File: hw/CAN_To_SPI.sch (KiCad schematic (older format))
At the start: 15 parts

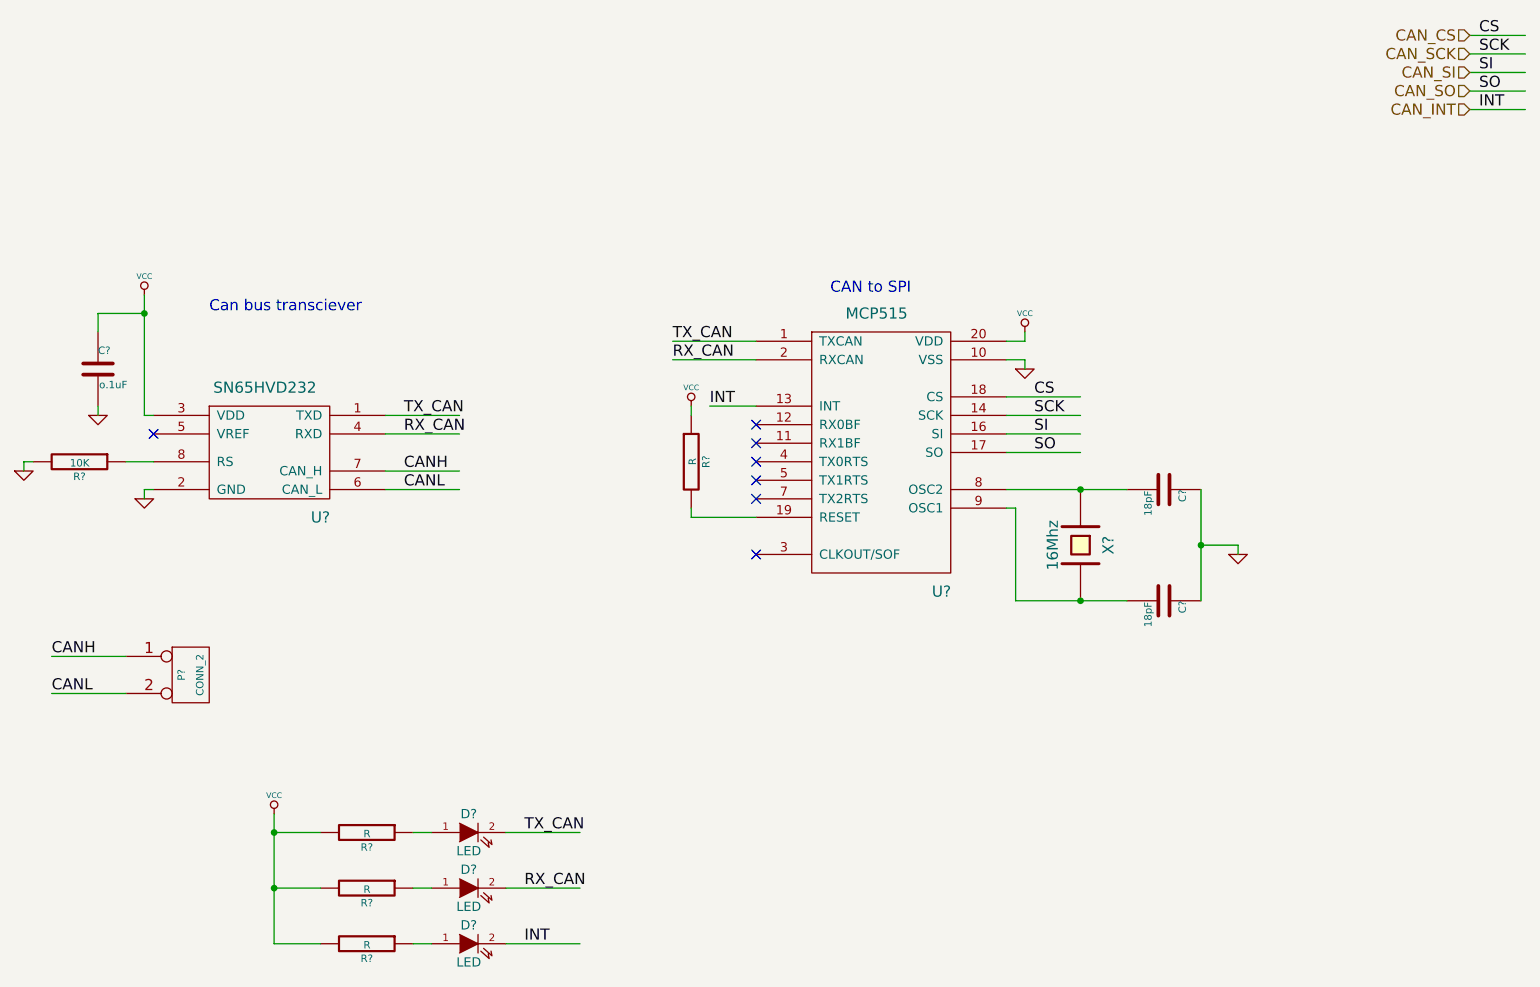
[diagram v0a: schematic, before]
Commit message: Added some of the netlist
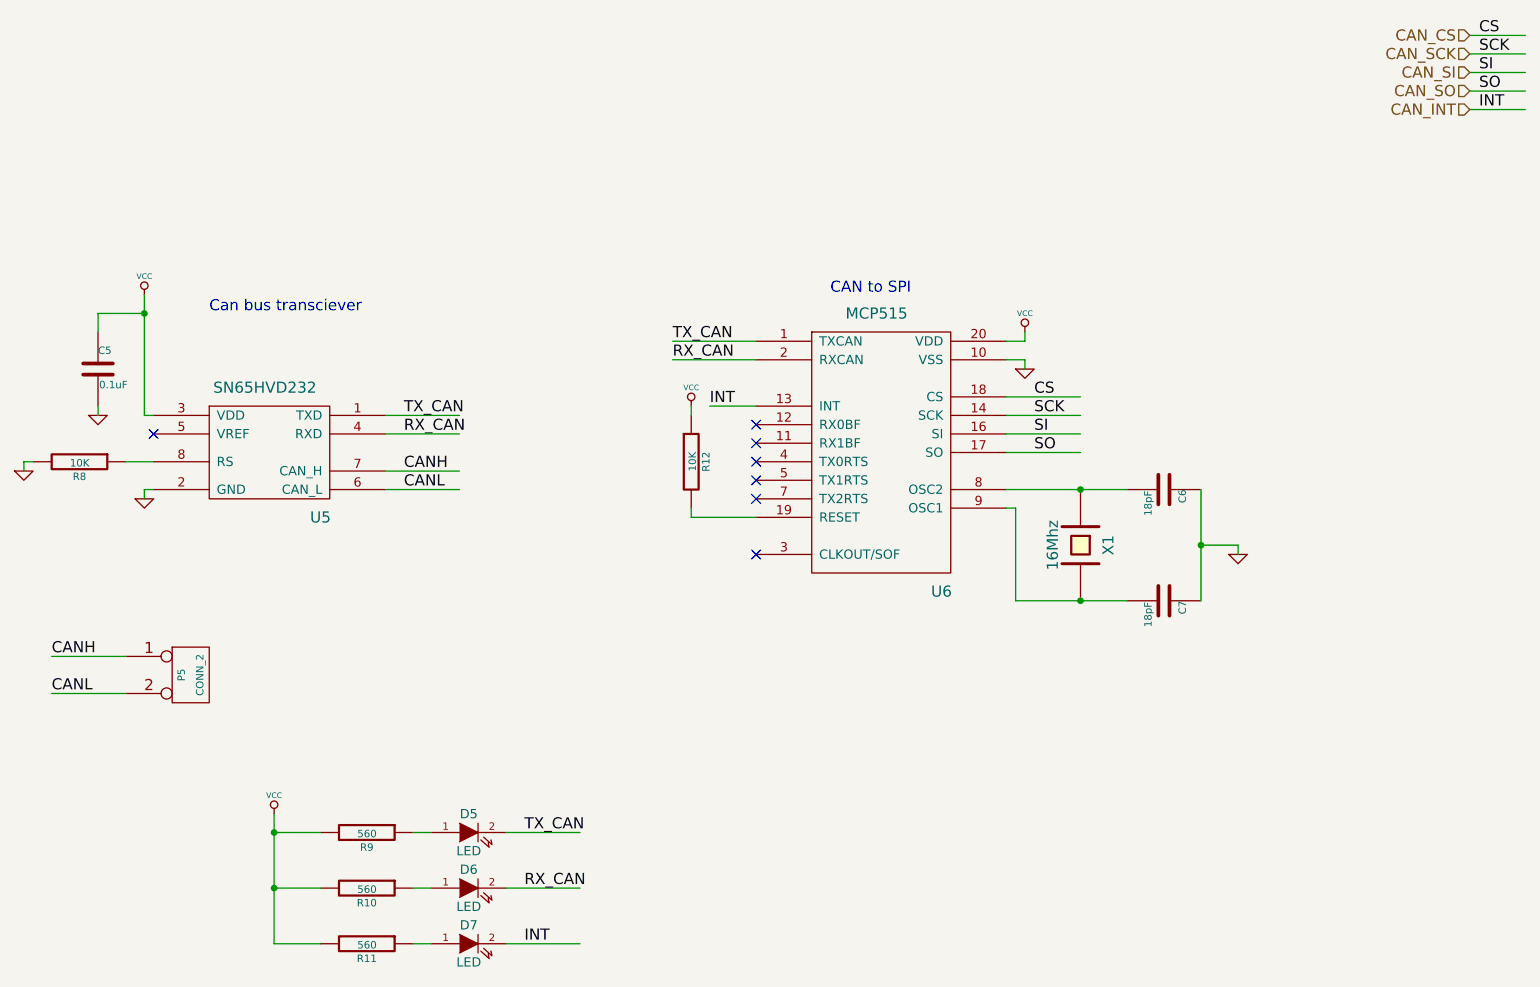
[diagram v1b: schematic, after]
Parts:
- C5: renamed from C?; value o.1uF -> 0.1uF
- R10, R11, R9: renamed from R?; value R -> 560
- R12: renamed from R?; value R -> 10K
- gave numbers to parts that had none: 10
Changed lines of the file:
@@
 LIBS:10to7_sensors
 LIBS:10to7_ic
+LIBS:Stepstick-cache
 EELAYER 24 0
 EELAYER END
@@
 $EndDescr
 $Comp
-L MCP2551 U?
+L MCP2551 U5
 U 1 1 538B0DEC
 P 3800 3600
-F 0 "U?" H 4100 3200 60  0000 C CNN
+F 0 "U5" H 4100 3200 60  0000 C CNN
 F 1 "SN65HVD232" H 3800 3900 60  0000 C CNN
 F 2 "" H 3800 3600 60  0000 C CNN
@@
 	3150 3850 3150 3900
 $Comp
-L GND #PWR?
+L GND #PWR031
 U 1 1 538B0DF4
 P 3150 3900
-F 0 "#PWR?" H 3150 3900 30  0001 C CNN
+F 0 "#PWR031" H 3150 3900 30  0001 C CNN
 F 1 "GND" H 3150 3830 30  0001 C CNN
 F 2 "" H 3150 3900 60  0000 C CNN
@@
 	3200 3700 3050 3700
 $Comp
-L R R?
+L R R8
 U 1 1 538B0DFD
 P 2800 3700
-F 0 "R?" V 2880 3700 40  0000 C CNN
+F 0 "R8" V 2880 3700 40  0000 C CNN
 F 1 "10K" V 2807 3701 40  0000 C CNN
 F 2 "" V 2730 3700 30  0000 C CNN
@@
 	2500 3700 2500 3750
 $Comp
-L GND #PWR?
+L GND #PWR032
 U 1 1 538B0E05
 P 2500 3750
-F 0 "#PWR?" H 2500 3750 30  0001 C CNN
+F 0 "#PWR032" H 2500 3750 30  0001 C CNN
 F 1 "GND" H 2500 3680 30  0001 C CNN
 F 2 "" H 2500 3750 60  0000 C CNN
@@
 RX_CAN
 $Comp
-L C C?
+L C C5
 U 1 1 538B0E14
 P 2900 3200
-F 0 "C?" H 2900 3300 40  0000 L CNN
-F 1 "o.1uF" H 2906 3115 40  0000 L CNN
+F 0 "C5" H 2900 3300 40  0000 L CNN
+F 1 "0.1uF" H 2906 3115 40  0000 L CNN
 F 2 "" H 2938 3050 30  0000 C CNN
 F 3 "" H 2900 3200 60  0000 C CNN
@@
 	2900 3400 2900 3450
 $Comp
-L GND #PWR?
+L GND #PWR033
 U 1 1 538B0E1E
 P 2900 3450
-F 0 "#PWR?" H 2900 3450 30  0001 C CNN
+F 0 "#PWR033" H 2900 3450 30  0001 C CNN
 F 1 "GND" H 2900 3380 30  0001 C CNN
 F 2 "" H 2900 3450 60  0000 C CNN
@@
 Can bus transciever
 $Comp
-L VCC #PWR?
+L VCC #PWR034
 U 1 1 538B0E25
 P 3150 2800
-F 0 "#PWR?" H 3150 2900 30  0001 C CNN
+F 0 "#PWR034" H 3150 2900 30  0001 C CNN
 F 1 "VCC" H 3150 2900 30  0000 C CNN
 F 2 "" H 3150 2800 60  0000 C CNN
@@
 $EndComp
 $Comp
-L MCP515 U?
+L MCP515 U6
 U 1 1 538B0E79
 P 6950 3300
-F 0 "U?" H 7450 2200 60  0000 C CNN
+F 0 "U6" H 7450 2200 60  0000 C CNN
 F 1 "MCP515" H 7100 3700 60  0000 C CNN
 F 2 "" H 6950 2750 60  0000 C CNN
@@
 	7900 3150 7900 3200
 $Comp
-L GND #PWR?
+L GND #PWR035
 U 1 1 538B0E8A
 P 7900 3200
-F 0 "#PWR?" H 7900 3200 30  0001 C CNN
+F 0 "#PWR035" H 7900 3200 30  0001 C CNN
 F 1 "GND" H 7900 3130 30  0001 C CNN
 F 2 "" H 7900 3200 60  0000 C CNN
@@
 	6100 4000 6100 3950
 $Comp
-L R R?
+L R R12
 U 1 1 538B0E92
 P 6100 3700
-F 0 "R?" V 6180 3700 40  0000 C CNN
-F 1 "R" V 6107 3701 40  0000 C CNN
+F 0 "R12" V 6180 3700 40  0000 C CNN
+F 1 "10K" V 6107 3701 40  0000 C CNN
 F 2 "" V 6030 3700 30  0000 C CNN
 F 3 "" H 6100 3700 30  0000 C CNN
@@
 	7900 3050 7900 3000
 $Comp
-L CRYSTAL X?
+L CRYSTAL X1
 U 1 1 538B0E9B
 P 8200 4150
-F 0 "X?" H 8200 4300 60  0000 C CNN
+F 0 "X1" H 8200 4300 60  0000 C CNN
 F 1 "16Mhz" H 8200 4000 60  0000 C CNN
 F 2 "" H 8200 4150 60  0000 C CNN
@@
 $EndComp
 $Comp
-L C C?
+L C C6
 U 1 1 538B0EA1
 P 8650 3850
-F 0 "C?" H 8650 3950 40  0000 L CNN
+F 0 "C6" H 8650 3950 40  0000 L CNN
 F 1 "18pF" H 8656 3765 40  0000 L CNN
 F 2 "" H 8688 3700 30  0000 C CNN
@@
 $EndComp
 $Comp
-L C C?
+L C C7
 U 1 1 538B0EA7
 P 8650 4450
-F 0 "C?" H 8650 4550 40  0000 L CNN
+F 0 "C7" H 8650 4550 40  0000 L CNN
 F 1 "18pF" H 8656 4365 40  0000 L CNN
 F 2 "" H 8688 4300 30  0000 C CNN
@@
 Connection ~ 8850 4150
 $Comp
-L GND #PWR?
+L GND #PWR036
 U 1 1 538B0EB3
 P 9050 4200
-F 0 "#PWR?" H 9050 4200 30  0001 C CNN
+F 0 "#PWR036" H 9050 4200 30  0001 C CNN
 F 1 "GND" H 9050 4130 30  0001 C CNN
 F 2 "" H 9050 4200 60  0000 C CNN
@@
 	7800 3350 8200 3350
 $Comp
-L VCC #PWR?
+L VCC #PWR037
 U 1 1 538B0EC1
 P 6100 3400
-F 0 "#PWR?" H 6100 3500 30  0001 C CNN
+F 0 "#PWR037" H 6100 3500 30  0001 C CNN
 F 1 "VCC" H 6100 3500 30  0000 C CNN
 F 2 "" H 6100 3400 60  0000 C CNN
@@
 $EndComp
 $Comp
-L VCC #PWR?
+L VCC #PWR038
 U 1 1 538B0EC7
 P 7900 3000
-F 0 "#PWR?" H 7900 3100 30  0001 C CNN
+F 0 "#PWR038" H 7900 3100 30  0001 C CNN
 F 1 "VCC" H 7900 3100 30  0000 C CNN
 F 2 "" H 7900 3000 60  0000 C CNN
@@
 CAN_SO
 $Comp
-L CONN_2 P?
+L CONN_2 P5
 U 1 1 538B1557
 P 3400 4850
-F 0 "P?" V 3350 4850 40  0000 C CNN
+F 0 "P5" V 3350 4850 40  0000 C CNN
 F 1 "CONN_2" V 3450 4850 40  0000 C CNN
 F 2 "" H 3400 4850 60  0000 C CNN
@@
 SO
 $Comp
-L LED D?
+L LED D5
 U 1 1 538B25BE
 P 4900 5700
-F 0 "D?" H 4900 5800 50  0000 C CNN
+F 0 "D5" H 4900 5800 50  0000 C CNN
 F 1 "LED" H 4900 5600 50  0000 C CNN
 F 2 "" H 4900 5700 60  0000 C CNN
@@
 $EndComp
 $Comp
-L R R?
+L R R9
 U 1 1 538B25D2
 P 4350 5700
-F 0 "R?" V 4430 5700 40  0000 C CNN
-F 1 "R" V 4357 5701 40  0000 C CNN
+F 0 "R9" V 4430 5700 40  0000 C CNN
+F 1 "560" V 4357 5701 40  0000 C CNN
 F 2 "" V 4280 5700 30  0000 C CNN
 F 3 "" H 4350 5700 30  0000 C CNN
@@
 TX_CAN
 $Comp
-L LED D?
+L LED D6
 U 1 1 538B2673
 P 4900 6000
-F 0 "D?" H 4900 6100 50  0000 C CNN
+F 0 "D6" H 4900 6100 50  0000 C CNN
 F 1 "LED" H 4900 5900 50  0000 C CNN
 F 2 "" H 4900 6000 60  0000 C CNN
@@
 $EndComp
 $Comp
-L R R?
+L R R10
 U 1 1 538B2679
 P 4350 6000
-F 0 "R?" V 4430 6000 40  0000 C CNN
-F 1 "R" V 4357 6001 40  0000 C CNN
+F 0 "R10" V 4430 6000 40  0000 C CNN
+F 1 "560" V 4357 6001 40  0000 C CNN
 F 2 "" V 4280 6000 30  0000 C CNN
 F 3 "" H 4350 6000 30  0000 C CNN
@@
 RX_CAN
 $Comp
-L LED D?
+L LED D7
 U 1 1 538B2687
 P 4900 6300
-F 0 "D?" H 4900 6400 50  0000 C CNN
+F 0 "D7" H 4900 6400 50  0000 C CNN
 F 1 "LED" H 4900 6200 50  0000 C CNN
 F 2 "" H 4900 6300 60  0000 C CNN
@@
 $EndComp
 $Comp
-L R R?
+L R R11
 U 1 1 538B268D
 P 4350 6300
-F 0 "R?" V 4430 6300 40  0000 C CNN
-F 1 "R" V 4357 6301 40  0000 C CNN
+F 0 "R11" V 4430 6300 40  0000 C CNN
+F 1 "560" V 4357 6301 40  0000 C CNN
 F 2 "" V 4280 6300 30  0000 C CNN
 F 3 "" H 4350 6300 30  0000 C CNN
@@
 INT
 $Comp
-L VCC #PWR?
+L VCC #PWR039
 U 1 1 538B270A
 P 3850 5600
-F 0 "#PWR?" H 3850 5700 30  0001 C CNN
+F 0 "#PWR039" H 3850 5700 30  0001 C CNN
 F 1 "VCC" H 3850 5700 30  0000 C CNN
 F 2 "" H 3850 5600 60  0000 C CNN

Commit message: corrected the CAN transceiver in the schematic - 3V3 version was selected incorrectly.
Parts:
- U5: value SN65HVD232 -> SN65HVD232_SN65HVD256
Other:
- note added: "Use 232 for 3.3V VCC and 256 for 5V VCC"
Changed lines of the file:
@@
 P 3800 3600
 F 0 "U5" H 4100 3200 60  0000 C CNN
-F 1 "SN65HVD232" H 3800 3900 60  0000 C CNN
+F 1 "SN65HVD232_SN65HVD256" H 3800 3900 60  0000 C CNN
 F 2 "" H 3800 3600 60  0000 C CNN
 F 3 "" H 3800 3600 60  0000 C CNN
@@
 Text Label 10350 1800 0    60   ~ 0
 INT
+Text Notes 2750 4150 0    60   ~ 0
+Use 232 for 3.3V VCC and 256 for 5V VCC
 $EndSCHEMATC
